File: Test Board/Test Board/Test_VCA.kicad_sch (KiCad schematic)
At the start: 57 parts, among them Q4 SST113, U31 OPA189, U32 OPA189, U33 OPA189, U35 LM13700, U36 OPA189, U37 VCA810

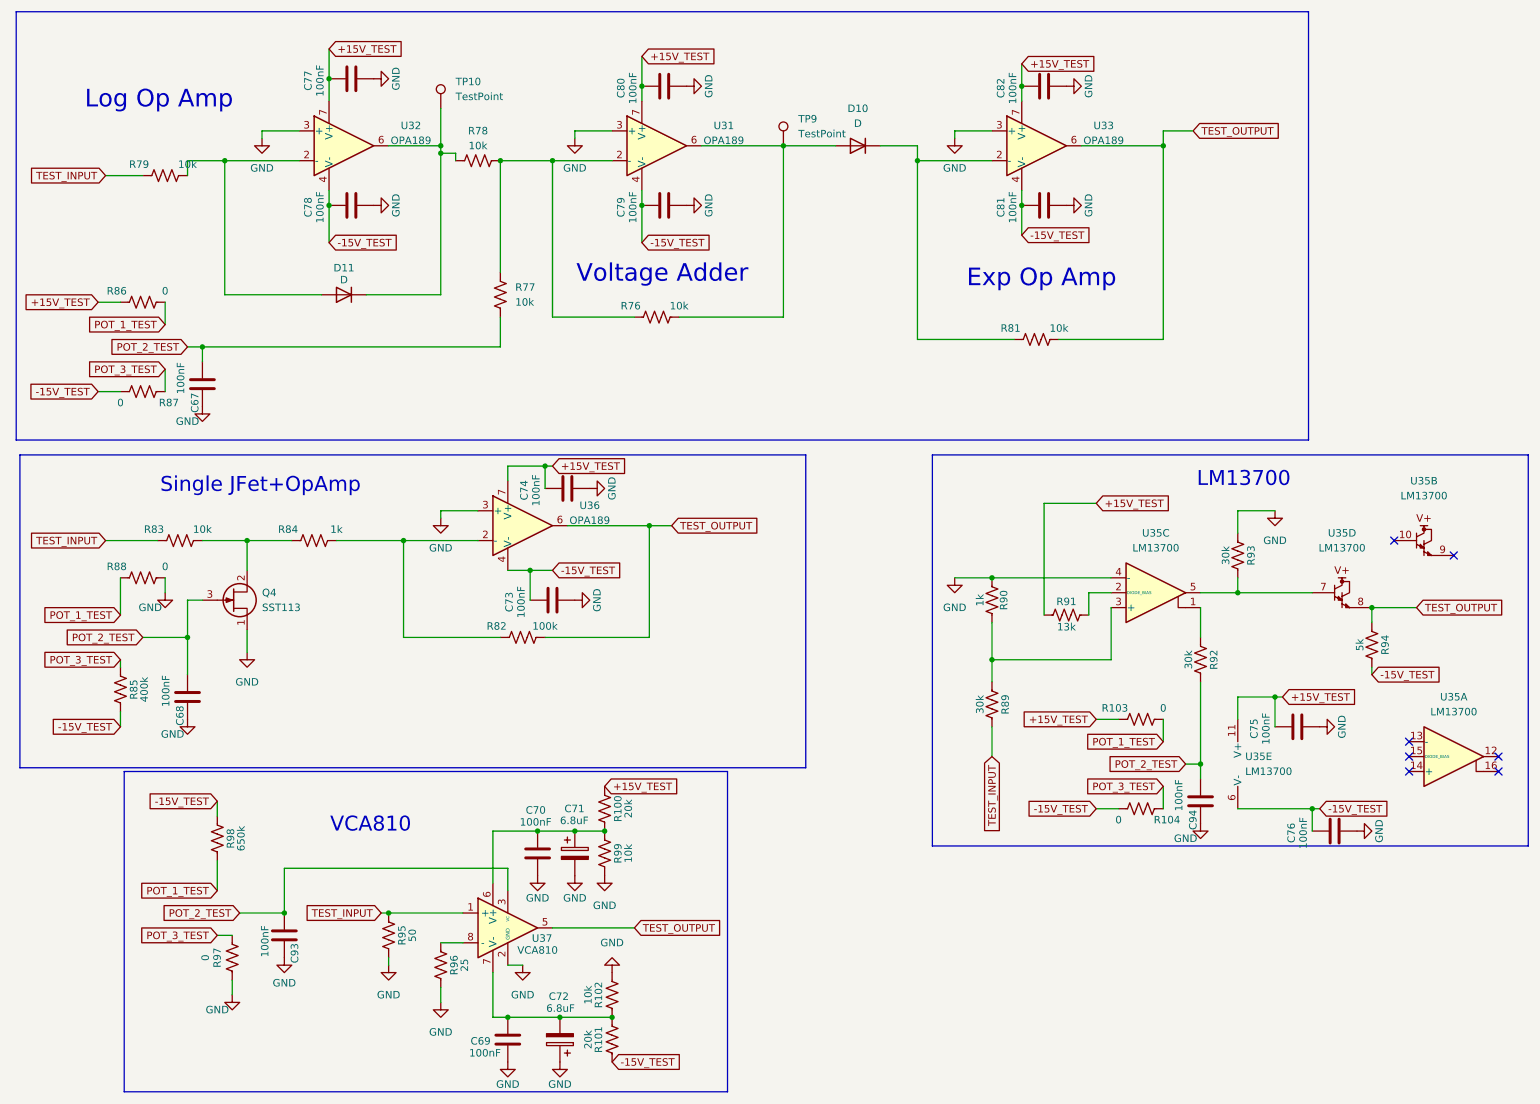
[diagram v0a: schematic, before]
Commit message: Removed LH circuit, added anti-windup test circuit, simplified voltage control mechanism
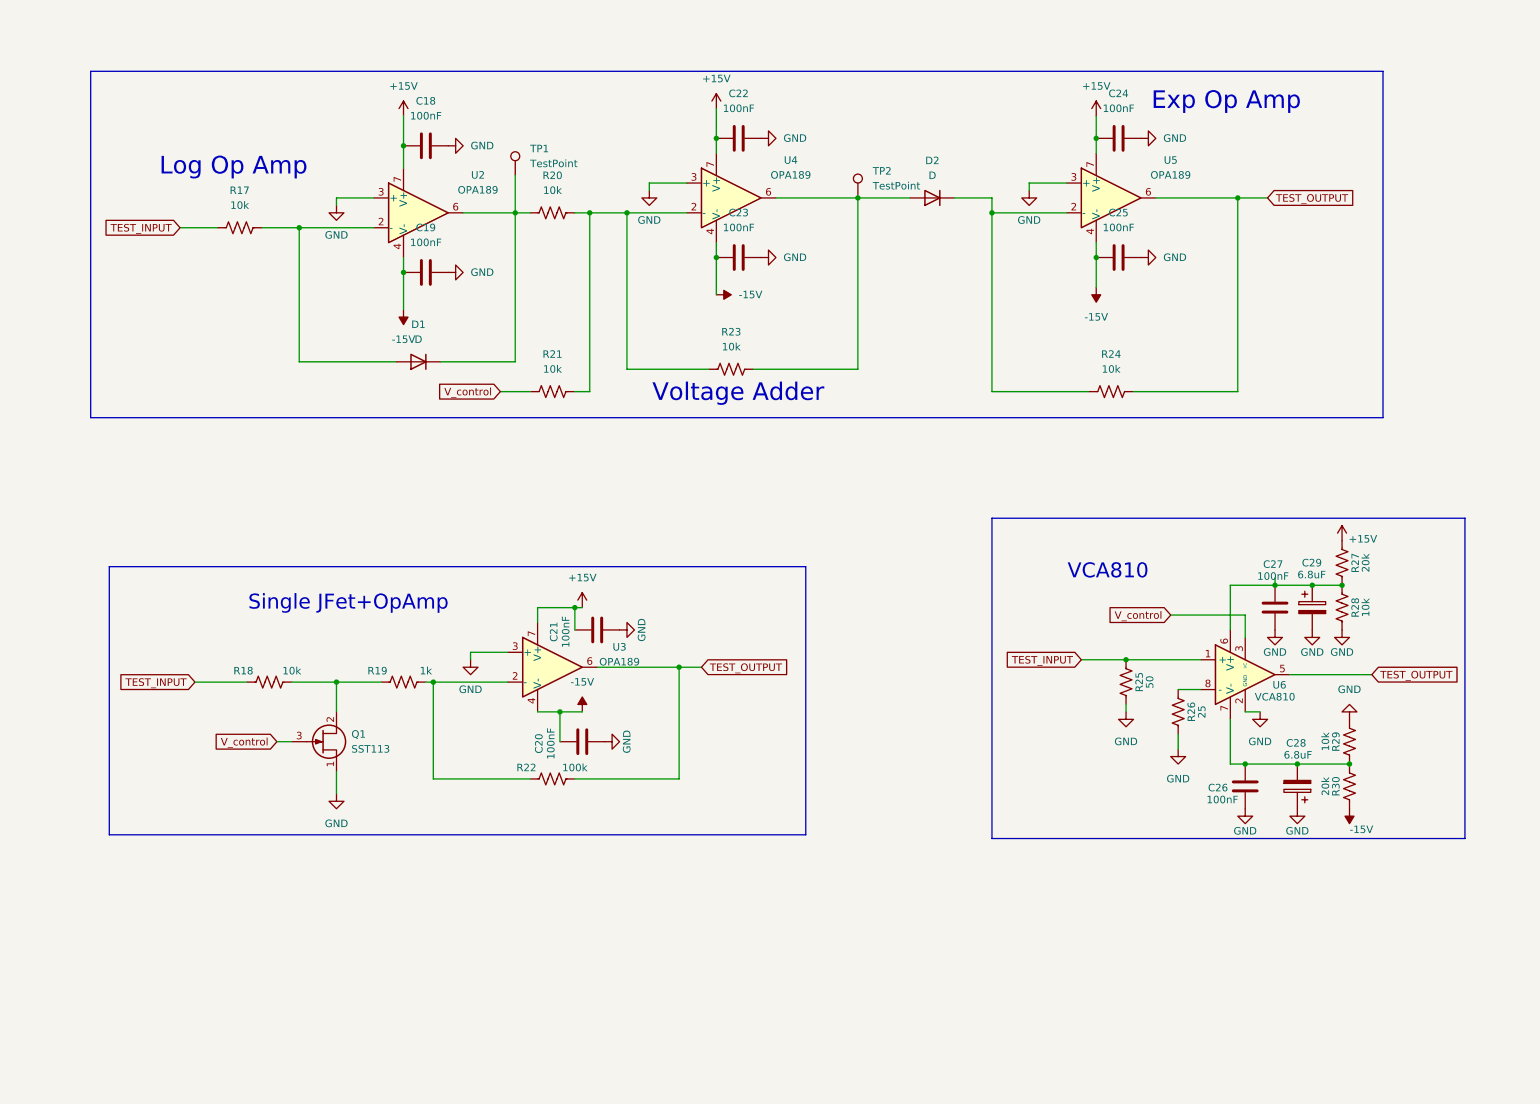
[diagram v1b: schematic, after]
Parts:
- removed C67, C68, C75, C76, C93, C94: 100nF, Capacitor_SMD:C_0805_2012Metric, symbol Device:C
- removed R103, R104, R86, R87, R88, R97: 0, Resistor_SMD:R_0805_2012Metric, symbol Device:R_US
- removed R77: 10k, Resistor_SMD:R_0805_2012Metric, symbol Device:R_US
- removed R85: 400k, Resistor_SMD:R_0805_2012Metric, symbol Device:R_US
- removed R89, R92, R93: 30k, Resistor_SMD:R_0805_2012Metric, symbol Device:R_US
- removed R90: 1k, Resistor_SMD:R_0805_2012Metric, symbol Device:R_US
- removed R91: 13k, Resistor_SMD:R_0805_2012Metric, symbol Device:R_US
- removed R94: 5k, Resistor_SMD:R_0805_2012Metric, symbol Device:R_US
- removed R98: 650k, Resistor_SMD:R_0805_2012Metric, symbol Device:R_US
- removed U35: LM13700, Package_SO:SOIC-16_3.9x9.9mm_P1.27mm, symbol Amplifier_Operational:LM13700
- added R21: 10k, Resistor_SMD:R_0805_2012Metric, symbol Device:R_US
- renumbered C77 to C18, C78 to C19, C73 to C20, C74 to C21, C80 to C22, C79 to C23, C82 to C24, C81 to C25, C69 to C26, C70 to C27, C72 to C28, C71 to C29, D11 to D1, D10 to D2, Q4 to Q1, R79 to R17, R83 to R18, R84 to R19, R78 to R20, R82 to R22, R76 to R23, R81 to R24, R95 to R25, R96 to R26, R100 to R27, R99 to R28, R102 to R29, R101 to R30, TP10 to TP1, TP9 to TP2, U32 to U2, U36 to U3, U31 to U4, U33 to U5, U37 to U6
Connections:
- net at R20.2, R23.1, U4.2 (-): now also R21.2
- net +15V_TEST renamed +15V
- net -15V_TEST renamed -15V
- net POT_2_TEST renamed V_control
- net V_control: now also R21.1
- no-connect marks 7 -> 0
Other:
- note removed: "LM13700"
- moved on the sheet: C18, C19, C20, C21, C22, C23, C24, C25, C26, C27, C28, C29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

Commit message: First pass at routing Test Board, TODO: Find and Double check Part numbers
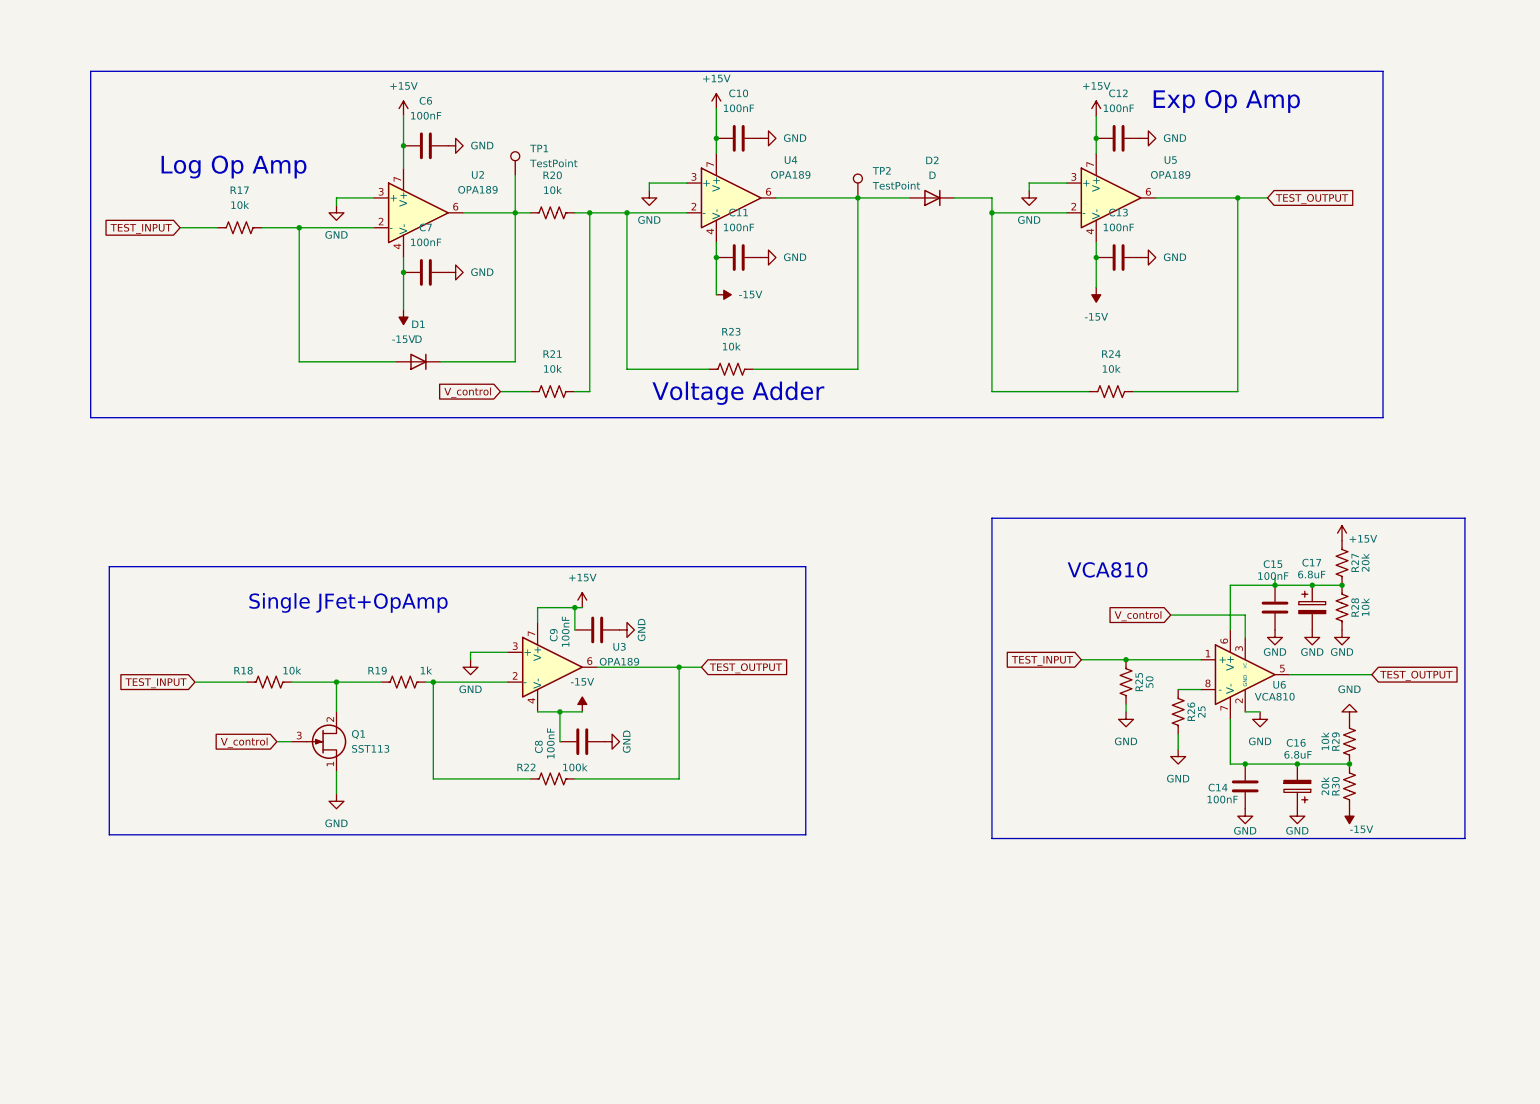
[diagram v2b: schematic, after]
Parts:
- renumbered C22 to C10, C23 to C11, C24 to C12, C25 to C13, C26 to C14, C27 to C15, C28 to C16, C29 to C17, C18 to C6, C19 to C7, C20 to C8, C21 to C9
